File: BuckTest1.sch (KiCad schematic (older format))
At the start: 22 parts, among them J1 POWERCONN, J2 POWERCONN, U1 LM3102

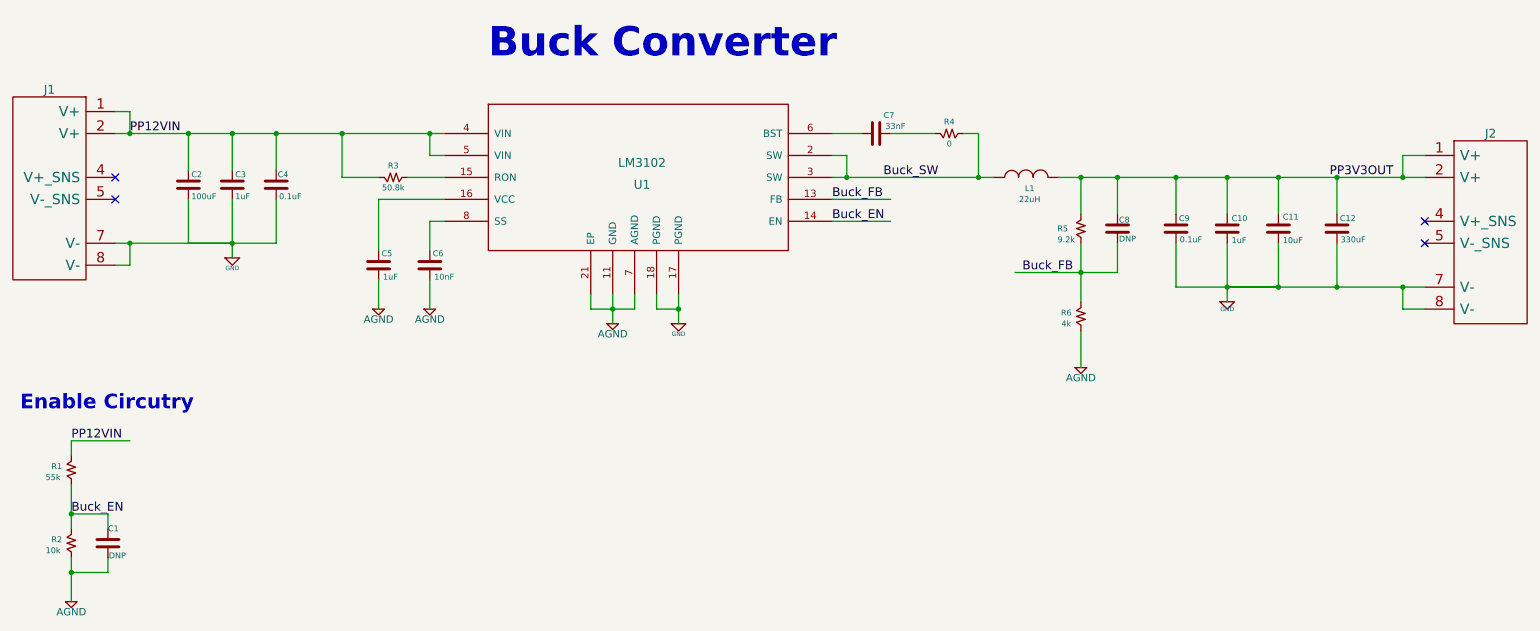
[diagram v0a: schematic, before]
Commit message: Create BOM + Update Component Values
Need to select new inductor due to non-stock at digikey
BOM created
Sch Values Updated
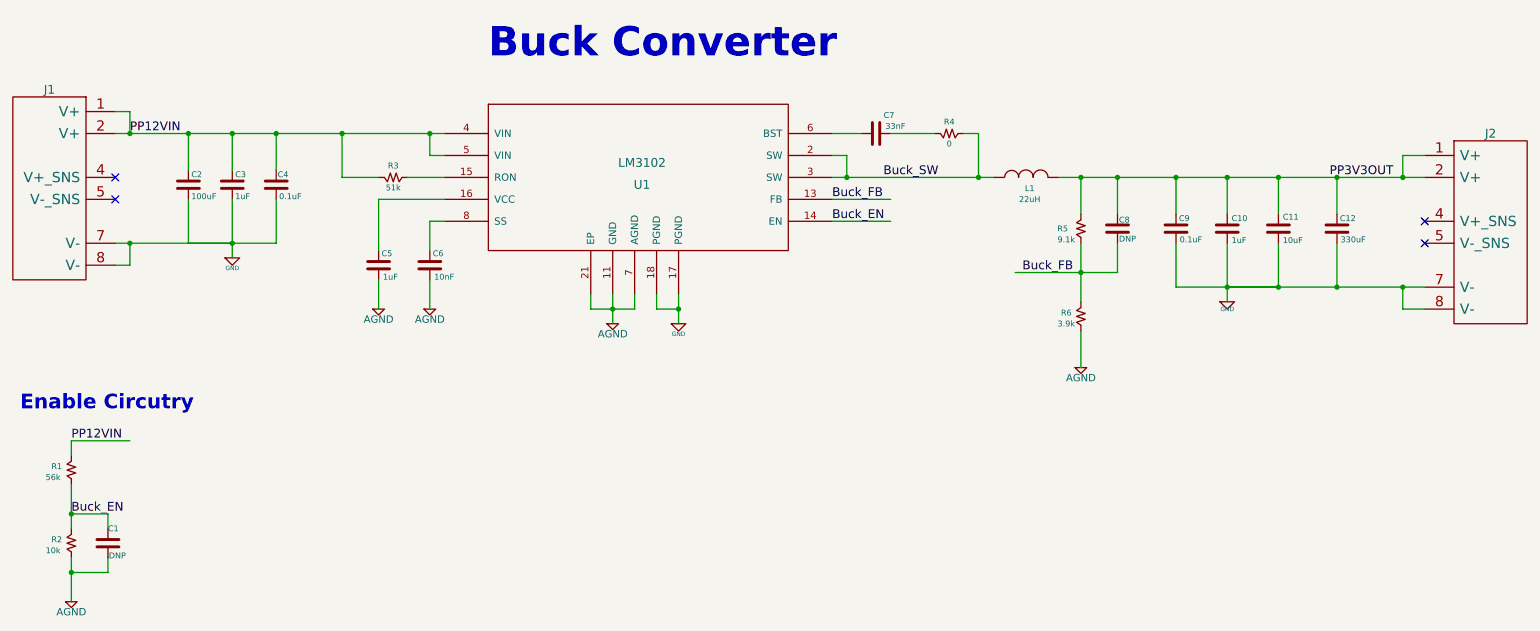
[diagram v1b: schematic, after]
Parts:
- C1, C10, C11, C5, C6, C7, C8, C9, R2, R4: footprint ~ -> 0603
- C12: footprint ~ -> D4
- C2: footprint ~ -> D3L
- C3, C4: footprint ~ -> 0603; Voltage (none) -> 25V
- J1, J2: footprint (none) -> 8x1 Pin Array
- L1: footprint ~ -> 4040DZ-11
- R1: value 55k -> 56k; footprint ~ -> 0603
- R3: value 50.8k -> 51k; footprint ~ -> 0603
- R5: value 9.2k -> 9.1k; footprint ~ -> 0603
- R6: value 4k -> 3.9k; footprint ~ -> 0603
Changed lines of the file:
@@
 Sheet 1 1
 Title "12V to 3.3V 2A Buck Converter 500kHz"
-Date "20 aug 2013"
+Date "21 aug 2013"
 Rev "1"
 Comp "Evil-inator"
@@
 F 0 "C9" H 8620 3920 40  0000 L CNN
 F 1 "0.1uF" H 8625 3775 40  0000 L CNN
-F 2 "~" H 8638 3700 30  0000 C CNN
+F 2 "0603" H 8638 3700 30  0001 C CNN
 F 3 "~" H 8600 3850 60  0000 C CNN
 	1    8600 3850
@@
 F 0 "C2" H 1870 3620 40  0000 L CNN
 F 1 "100uF" H 1870 3470 40  0000 L CNN
-F 2 "~" H 1888 3400 30  0000 C CNN
-F 3 "~" H 1850 3550 60  0000 C CNN
+F 2 "D3L" H 1888 3400 30  0001 C CNN
+F 3 "20TQC100MYF" H 1850 3300 60  0001 C CNN
 	1    1850 3550
 	1    0    0    -1
@@
 F 0 "C5" H 3170 4180 40  0000 L CNN
 F 1 "1uF" H 3180 4020 40  0000 L CNN
-F 2 "~" H 3188 3950 30  0000 C CNN
+F 2 "0603" H 3188 3950 30  0001 C CNN
 F 3 "~" H 3150 4100 60  0000 C CNN
 	1    3150 4100
@@
 F 0 "C6" H 3520 4180 40  0000 L CNN
 F 1 "10nF" H 3530 4020 40  0000 L CNN
-F 2 "~" H 3538 3950 30  0000 C CNN
+F 2 "0603" H 3538 3950 30  0001 C CNN
 F 3 "~" H 3500 4100 60  0000 C CNN
 	1    3500 4100
@@
 F 0 "C7" V 6675 3075 40  0000 L CNN
 F 1 "33nF" V 6600 3000 40  0000 L CNN
-F 2 "~" H 6588 3050 30  0000 C CNN
+F 2 "0603" H 6588 3050 30  0001 C CNN
 F 3 "~" H 6550 3200 60  0000 C CNN
 	1    6550 3200
@@
 P 7950 3750
 F 0 "R5" H 7825 3650 40  0000 C CNN
-F 1 "9.2k" H 7850 3575 40  0000 C CNN
-F 2 "~" V 7880 3750 30  0000 C CNN
+F 1 "9.1k" H 7850 3575 40  0000 C CNN
+F 2 "0603" V 7880 3750 30  0001 C CNN
 F 3 "~" H 7950 3510 30  0000 C CNN
 	1    7950 3750
@@
 P 7950 4350
 F 0 "R6" H 7850 4275 40  0000 C CNN
-F 1 "4k" H 7850 4200 40  0000 C CNN
-F 2 "~" V 7880 4350 30  0000 C CNN
+F 1 "3.9k" H 7850 4200 40  0000 C CNN
+F 2 "0603" V 7880 4350 30  0001 C CNN
 F 3 "~" H 7950 4110 30  0000 C CNN
 	1    7950 4350
@@
 P 3150 3500
 F 0 "R3" V 3230 3400 40  0000 C CNN
-F 1 "50.8k" V 3080 3400 40  0000 C CNN
-F 2 "~" V 3080 3500 30  0000 C CNN
+F 1 "51k" V 3080 3400 40  0000 C CNN
+F 2 "0603" V 3080 3500 30  0001 C CNN
 F 3 "~" H 3150 3260 30  0000 C CNN
 	1    3150 3500
@@
 F 0 "L1" V 7275 3250 40  0000 C CNN
 F 1 "22uH" V 7200 3250 40  0000 C CNN
-F 2 "~" H 7350 3200 60  0000 C CNN
+F 2 "4040DZ-11" H 7350 3200 60  0001 C CNN
 F 3 "~" H 7350 3200 60  0000 C CNN
 	1    7350 3500
@@
 F 0 "C10" H 8980 3920 40  0000 L CNN
 F 1 "1uF" H 8980 3770 40  0000 L CNN
-F 2 "~" H 8988 3700 30  0000 C CNN
+F 2 "0603" H 8988 3700 30  0001 C CNN
 F 3 "~" H 8950 3850 60  0000 C CNN
 	1    8950 3850
@@
 F 0 "C11" H 9330 3930 40  0000 L CNN
 F 1 "10uF" H 9330 3770 40  0000 L CNN
-F 2 "~" H 9338 3700 30  0000 C CNN
+F 2 "0603" H 9338 3700 30  0001 C CNN
 F 3 "~" H 9300 3850 60  0000 C CNN
 	1    9300 3850
@@
 F 0 "R4" V 7030 3100 40  0000 C CNN
 F 1 "0" V 6880 3100 40  0000 C CNN
-F 2 "~" V 6880 3200 30  0000 C CNN
+F 2 "0603" V 6880 3200 30  0001 C CNN
 F 3 "~" H 6950 2960 30  0000 C CNN
 	1    6950 3200
@@
 F 0 "J1" H 1800 3000 60  0000 C CNN
 F 1 "POWERCONN" H 1800 3100 60  0001 C CNN
-F 2 "" H 1350 2950 60  0000 C CNN
+F 2 "8x1 Pin Array" H 1350 2950 60  0001 C CNN
 F 3 "" H 1350 2950 60  0000 C CNN
 	1    1350 2950
@@
 F 0 "J2" H 10750 3300 60  0000 C CNN
 F 1 "POWERCONN" H 10750 3400 60  0001 C CNN
-F 2 "" H 10300 3250 60  0000 C CNN
+F 2 "8x1 Pin Array" H 10300 3250 60  0001 C CNN
 F 3 "" H 10300 3250 60  0000 C CNN
 	1    10300 3250
@@
 F 0 "C3" H 2170 3620 40  0000 L CNN
 F 1 "1uF" H 2170 3470 40  0000 L CNN
-F 2 "~" H 2188 3400 30  0000 C CNN
+F 2 "0603" H 2188 3400 30  0001 C CNN
 F 3 "~" H 2150 3550 60  0000 C CNN
+F 4 "25V" H 2150 3550 60  0001 C CNN "Voltage"
 	1    2150 3550
 	1    0    0    -1
@@
 F 0 "C4" H 2460 3620 40  0000 L CNN
 F 1 "0.1uF" H 2470 3470 40  0000 L CNN
-F 2 "~" H 2488 3400 30  0000 C CNN
+F 2 "0603" H 2488 3400 30  0001 C CNN
 F 3 "~" H 2450 3550 60  0000 C CNN
+F 4 "25V" H 2450 3550 60  0001 C CNN "Voltage"
 	1    2450 3550
 	1    0    0    -1
@@
 P 1050 5400
 F 0 "R1" H 950 5325 40  0000 C CNN
-F 1 "55k" H 925 5250 40  0000 C CNN
-F 2 "~" V 980 5400 30  0000 C CNN
+F 1 "56k" H 925 5250 40  0000 C CNN
+F 2 "0603" V 980 5400 30  0001 C CNN
 F 3 "~" H 1050 5160 30  0000 C CNN
 	1    1050 5400
@@
 F 0 "C1" H 1300 6100 40  0000 L CNN
 F 1 "DNP" H 1306 5915 40  0000 L CNN
-F 2 "~" H 1338 5850 30  0000 C CNN
+F 2 "0603" H 1338 5850 30  0001 C CNN
 F 3 "~" H 1300 6000 60  0000 C CNN
 	1    1300 6000
@@
 F 0 "R2" H 950 5825 40  0000 C CNN
 F 1 "10k" H 925 5750 40  0000 C CNN
-F 2 "~" V 980 5900 30  0000 C CNN
+F 2 "0603" V 980 5900 30  0001 C CNN
 F 3 "~" H 1050 5660 30  0000 C CNN
 	1    1050 5900
@@
 F 0 "C8" H 8210 3910 40  0000 L CNN
 F 1 "DNP" H 8210 3780 40  0000 L CNN
-F 2 "~" H 8238 3700 30  0000 C CNN
+F 2 "0603" H 8238 3700 30  0001 C CNN
 F 3 "~" H 8200 3850 60  0000 C CNN
 	1    8200 3850
@@
 F 0 "C12" H 9720 3920 40  0000 L CNN
 F 1 "330uF" H 9725 3775 40  0000 L CNN
-F 2 "~" H 9738 3700 30  0000 C CNN
-F 3 "~" H 9700 3850 60  0000 C CNN
+F 2 "D4" H 9738 3700 30  0001 C CNN
+F 3 "6TPE330MAA" H 9700 3850 60  0001 C CNN
 	1    9700 3850
 	1    0    0    -1

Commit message: Finalized Component / Footprint Selection
Schematic and preliminary BOM complete. Layout is next step.
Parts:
- L1: footprint 4040DZ-11 -> SRR1280
- U1: footprint ~ -> HTSSOP
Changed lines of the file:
@@
 F 0 "U1" H 4950 2850 60  0000 C CNN
 F 1 "LM3102" H 4950 3000 60  0000 C CNN
-F 2 "~" H 4450 3350 60  0000 C CNN
-F 3 "~" H 4450 3350 60  0000 C CNN
+F 2 "HTSSOP" H 4450 3350 60  0001 C CNN
+F 3 "LM3102MHX/NOPB" H 4450 3350 60  0001 C CNN
 	1    3600 3200
 	1    0    0    -1
@@
 F 1 "0.1uF" H 8625 3775 40  0000 L CNN
 F 2 "0603" H 8638 3700 30  0001 C CNN
-F 3 "~" H 8600 3850 60  0000 C CNN
+F 3 "GRM188F51E104ZA01D" H 8600 3850 60  0001 C CNN
 	1    8600 3850
 	1    0    0    -1
@@
 F 1 "1uF" H 3180 4020 40  0000 L CNN
 F 2 "0603" H 3188 3950 30  0001 C CNN
-F 3 "~" H 3150 4100 60  0000 C CNN
+F 3 "GRM188F51E105ZA12D" H 3150 4100 60  0001 C CNN
 	1    3150 4100
 	1    0    0    -1
@@
 F 1 "10nF" H 3530 4020 40  0000 L CNN
 F 2 "0603" H 3538 3950 30  0001 C CNN
-F 3 "~" H 3500 4100 60  0000 C CNN
+F 3 "GRM188R71E103KA01D" H 3500 4100 60  0001 C CNN
 	1    3500 4100
 	1    0    0    -1
@@
 F 1 "33nF" V 6600 3000 40  0000 L CNN
 F 2 "0603" H 6588 3050 30  0001 C CNN
-F 3 "~" H 6550 3200 60  0000 C CNN
+F 3 "GRM188R71E333KA01D" H 6550 3200 60  0001 C CNN
 	1    6550 3200
 	0    -1   -1   0
@@
 F 1 "9.1k" H 7850 3575 40  0000 C CNN
 F 2 "0603" V 7880 3750 30  0001 C CNN
-F 3 "~" H 7950 3510 30  0000 C CNN
+F 3 "ERJ-3EKF9101V" H 7950 3510 30  0001 C CNN
 	1    7950 3750
 	1    0    0    -1
@@
 F 1 "3.9k" H 7850 4200 40  0000 C CNN
 F 2 "0603" V 7880 4350 30  0001 C CNN
-F 3 "~" H 7950 4110 30  0000 C CNN
+F 3 "ERJ-3EKF3902V" H 7950 4110 30  0001 C CNN
 	1    7950 4350
 	1    0    0    -1
@@
 F 0 "L1" V 7275 3250 40  0000 C CNN
 F 1 "22uH" V 7200 3250 40  0000 C CNN
-F 2 "4040DZ-11" H 7350 3200 60  0001 C CNN
-F 3 "~" H 7350 3200 60  0000 C CNN
+F 2 "SRR1280" H 7350 3200 60  0001 C CNN
+F 3 "SRR1280-220M" H 7350 3200 60  0001 C CNN
 	1    7350 3500
 	0    -1   -1   0
@@
 F 1 "1uF" H 8980 3770 40  0000 L CNN
 F 2 "0603" H 8988 3700 30  0001 C CNN
-F 3 "~" H 8950 3850 60  0000 C CNN
+F 3 "GRM188R60J105KA01D" H 8950 3850 60  0001 C CNN
 	1    8950 3850
 	1    0    0    -1
@@
 F 1 "10uF" H 9330 3770 40  0000 L CNN
 F 2 "0603" H 9338 3700 30  0001 C CNN
-F 3 "~" H 9300 3850 60  0000 C CNN
+F 3 "GRM188R60J106ME47D" H 9300 3850 60  0001 C CNN
 	1    9300 3850
 	1    0    0    -1
@@
 F 1 "0" V 6880 3100 40  0000 C CNN
 F 2 "0603" V 6880 3200 30  0001 C CNN
-F 3 "~" H 6950 2960 30  0000 C CNN
+F 3 "ERJ-3GEY0R00V" H 6950 2960 30  0001 C CNN
 	1    6950 3200
 	0    -1   -1   0
@@
 F 1 "POWERCONN" H 1800 3100 60  0001 C CNN
 F 2 "8x1 Pin Array" H 1350 2950 60  0001 C CNN
-F 3 "" H 1350 2950 60  0000 C CNN
+F 3 "68002-408HLF" H 1350 2950 60  0001 C CNN
 	1    1350 2950
 	-1   0    0    -1
@@
 F 1 "POWERCONN" H 10750 3400 60  0001 C CNN
 F 2 "8x1 Pin Array" H 10300 3250 60  0001 C CNN
-F 3 "" H 10300 3250 60  0000 C CNN
+F 3 "68002-408HLF" H 10300 3250 60  0001 C CNN
 	1    10300 3250
 	1    0    0    -1
@@
 F 1 "1uF" H 2170 3470 40  0000 L CNN
 F 2 "0603" H 2188 3400 30  0001 C CNN
-F 3 "~" H 2150 3550 60  0000 C CNN
+F 3 "GRM188F51E105ZA12D" H 2150 3550 60  0001 C CNN
 F 4 "25V" H 2150 3550 60  0001 C CNN "Voltage"
 	1    2150 3550
@@
 F 1 "0.1uF" H 2470 3470 40  0000 L CNN
 F 2 "0603" H 2488 3400 30  0001 C CNN
-F 3 "~" H 2450 3550 60  0000 C CNN
+F 3 "GRM188F51E104ZA01D" H 2450 3550 60  0001 C CNN
 F 4 "25V" H 2450 3550 60  0001 C CNN "Voltage"
 	1    2450 3550
@@
 F 1 "56k" H 925 5250 40  0000 C CNN
 F 2 "0603" V 980 5400 30  0001 C CNN
-F 3 "~" H 1050 5160 30  0000 C CNN
+F 3 "ERJ-3EKF5602V" H 1050 5160 30  0001 C CNN
 	1    1050 5400
 	1    0    0    -1
@@
 F 1 "10k" H 925 5750 40  0000 C CNN
 F 2 "0603" V 980 5900 30  0001 C CNN
-F 3 "~" H 1050 5660 30  0000 C CNN
+F 3 "ERJ-3EKF1002V" H 1050 5660 30  0001 C CNN
 	1    1050 5900
 	1    0    0    -1

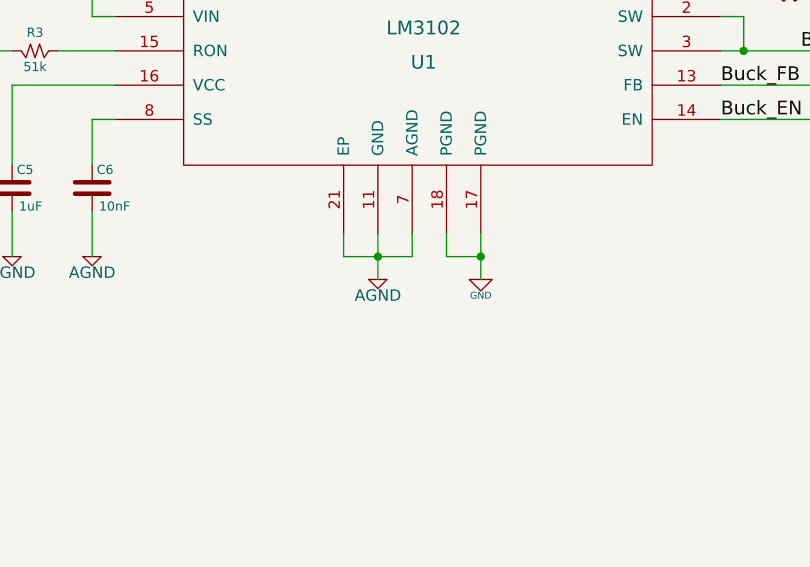
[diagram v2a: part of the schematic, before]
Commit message: Created PCB
Altered schematic to connect GND planes.
Created layout, single layer implementation not possible
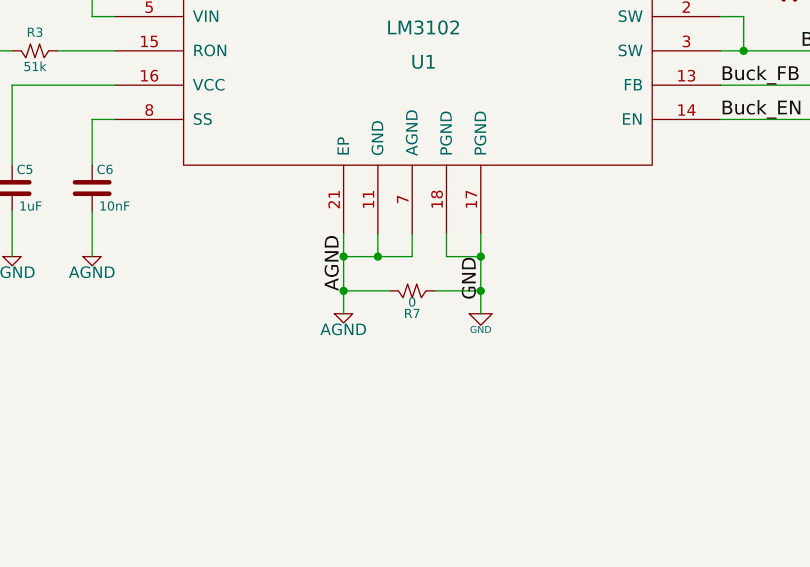
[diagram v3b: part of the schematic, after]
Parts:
- added R7: 0, ~, symbol R
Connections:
- wire segments 69 -> 71
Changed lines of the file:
@@
 Sheet 1 1
 Title "12V to 3.3V 2A Buck Converter 500kHz"
-Date "21 aug 2013"
+Date "22 aug 2013"
 Rev "1"
 Comp "Evil-inator"
@@
 L GND #PWR01
 U 1 1 520E7056
-P 5200 4500
-F 0 "#PWR01" H 5200 4500 30  0001 C CNN
-F 1 "GND" H 5200 4430 30  0000 C CNN
-F 2 "~" H 5200 4500 60  0000 C CNN
-F 3 "~" H 5200 4500 60  0000 C CNN
-	1    5200 4500
+P 5200 4650
+F 0 "#PWR01" H 5200 4650 30  0001 C CNN
+F 1 "GND" H 5200 4580 30  0000 C CNN
+F 2 "~" H 5200 4650 60  0000 C CNN
+F 3 "~" H 5200 4650 60  0000 C CNN
+	1    5200 4650
 	1    0    0    -1
 $EndComp
@@
 L AGND #PWR02
 U 1 1 520E7065
-P 4750 4500
-F 0 "#PWR02" H 4750 4500 40  0001 C CNN
-F 1 "AGND" H 4750 4430 50  0000 C CNN
-F 2 "~" H 4750 4500 60  0000 C CNN
-F 3 "~" H 4750 4500 60  0000 C CNN
-	1    4750 4500
+P 4600 4650
+F 0 "#PWR02" H 4600 4650 40  0001 C CNN
+F 1 "AGND" H 4600 4580 50  0000 C CNN
+F 2 "~" H 4600 4650 60  0000 C CNN
+F 3 "~" H 4600 4650 60  0000 C CNN
+	1    4600 4650
 	1    0    0    -1
 $EndComp
@@
 Buck_EN
 Wire Wire Line
-	4600 4300 4600 4400
-Wire Wire Line
-	4600 4400 4900 4400
-Wire Wire Line
-	4900 4400 4900 4300
-Wire Wire Line
-	4750 4300 4750 4500
-Connection ~ 4750 4400
+	4600 4300 4600 4650
 Wire Wire Line
 	5050 4300 5050 4400
@@
 	5050 4400 5200 4400
 Wire Wire Line
-	5200 4300 5200 4500
+	5200 4300 5200 4650
 Wire Wire Line
 	1350 3200 3600 3200
@@
 	9700 3950 9700 4250
 Connection ~ 9700 4250
+$Comp
+L R R7
+U 1 1 52165AA1
+P 4800 4550
+F 0 "R7" V 4700 4450 40  0000 C CNN
+F 1 "0" V 4750 4450 40  0000 C CNN
+F 2 "~" V 4730 4550 30  0000 C CNN
+F 3 "~" H 4800 4310 30  0000 C CNN
+	1    4800 4550
+	0    -1   -1   0
+$EndComp
+Wire Wire Line
+	4800 4550 4600 4550
+Connection ~ 4600 4550
+Wire Wire Line
+	5000 4550 5200 4550
+Connection ~ 5200 4550
+Text Label 4600 4550 1    60   ~ 0
+AGND
+Text Label 5200 4400 3    60   ~ 0
+GND
+Wire Wire Line
+	4750 4300 4750 4400
+Wire Wire Line
+	4600 4400 4900 4400
+Connection ~ 4600 4400
+Wire Wire Line
+	4900 4400 4900 4300
+Connection ~ 4750 4400
 $EndSCHEMATC
